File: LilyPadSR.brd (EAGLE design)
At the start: 100 x 50.9 mm, 40 parts, among them IC1 74HC595D, IC2 74HC595D

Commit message: alignment and routing
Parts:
- moved U$21 18.3 mm to (25.4, 76.8), turned to 270 degrees
- moved U$18 6.15 mm to (31.5, 75.9), turned to 253.7 degrees
- moved U$22 6.06 mm to (37.2, 73.4), turned to 237.4 degrees
- moved U$19 6.01 mm to (42.0, 69.3), turned to 221.1 degrees
- moved R13 2.75 mm to (32.8, 42.2)
- moved R16 2.54 mm to (39.6, 52.6)
- moved U$14 2.43 mm to (37.2, 35.8)
- moved U$15 2.37 mm to (42.0, 39.9)
- moved R15 2.34 mm to (38.6, 48.5)
- moved R14 2.17 mm to (36.3, 45.0)
- moved IC1 1.80 mm to (25.4, 59.7)
- moved IC2 1.80 mm to (25.4, 49.5)
- moved U$5 1.80 mm to (5.33, 64.0)
- moved U$16 1.80 mm to (45.5, 45.2)
- moved R12 1.63 mm to (29.2, 40.9)
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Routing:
- net VCC: track 0.00 -> 46.4 mm, vias 0 -> 4
- net GND: track 0.00 -> 44.9 mm
- net SRCLK: track 0.00 -> 23.0 mm
- net S_OUT: track 0.00 -> 19.2 mm
- net SER: track 0.00 -> 17.9 mm
- net RCLK: track 0.00 -> 17.7 mm
- net N$16: track 0.00 -> 15.1 mm, vias 0 -> 2
- net N$15: track 0.00 -> 14.4 mm
- net N$14: track 0.00 -> 13.7 mm
- net N$9: track 0.00 -> 13.4 mm
- net N$8: track 0.00 -> 12.9 mm
- net N$7: track 0.00 -> 12.4 mm
- net N$13: track 0.00 -> 11.7 mm
- net N$6: track 0.00 -> 10.7 mm
- net N$5: track 0.00 -> 10.4 mm
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
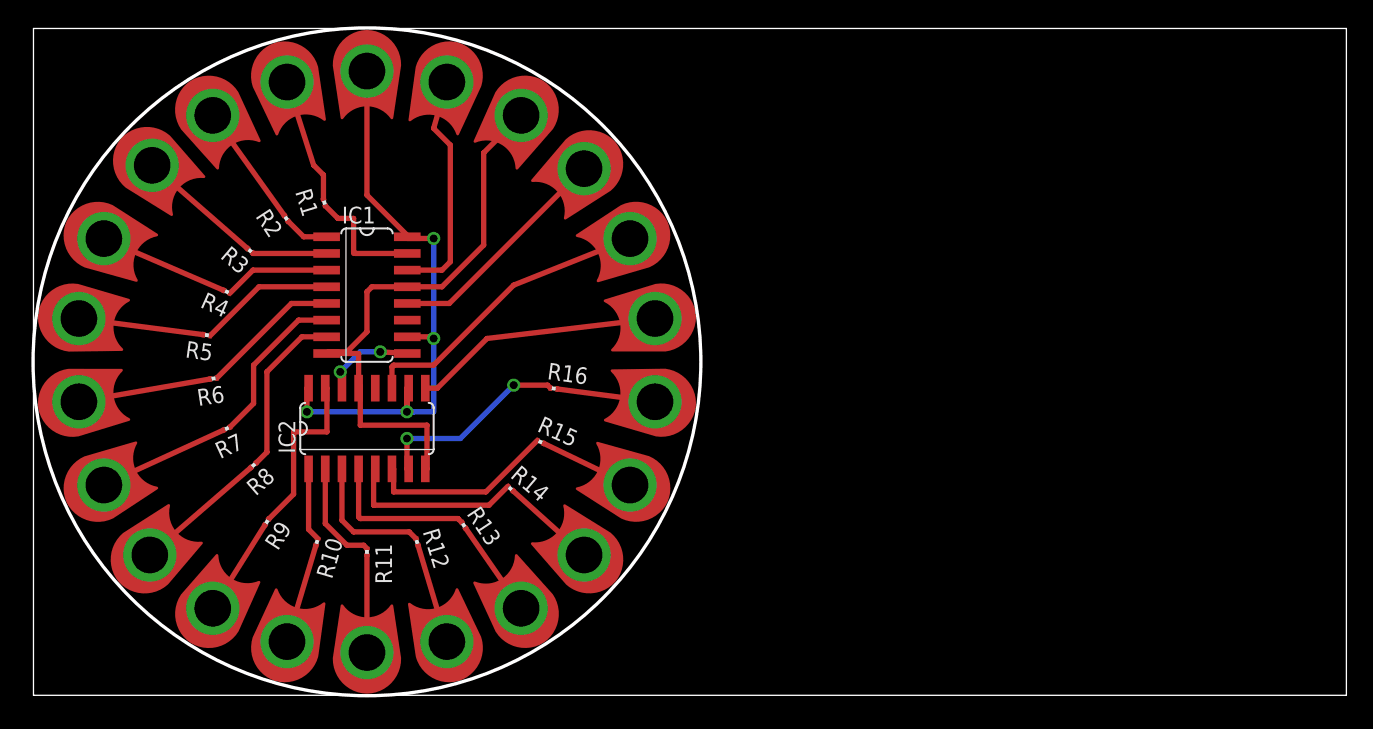
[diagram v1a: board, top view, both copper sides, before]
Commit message: removed right angles
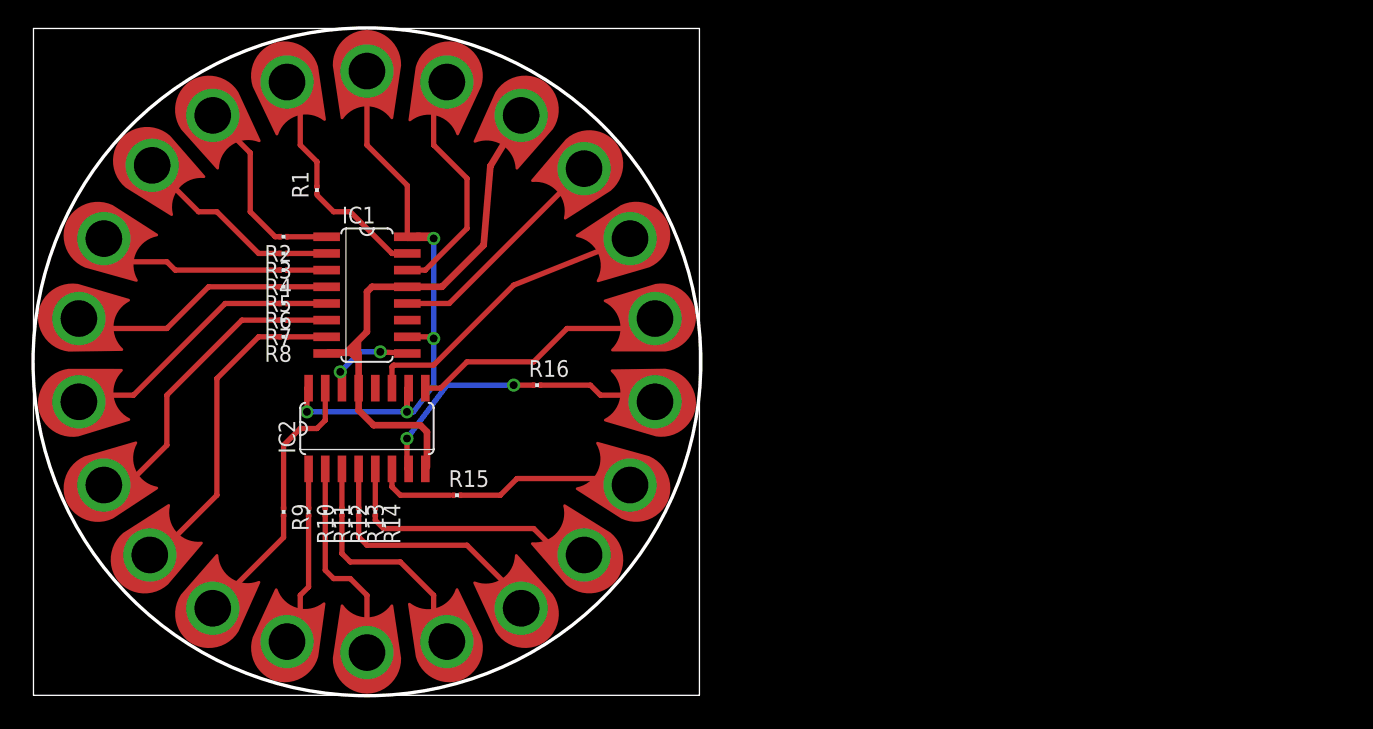
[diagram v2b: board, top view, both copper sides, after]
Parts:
- moved R14 10.4 mm to (26.0, 43.2), turned to 270 degrees
- moved R8 10.0 mm to (19.1, 56.5), turned to 180 degrees
- moved R7 9.32 mm to (19.1, 57.8), turned to 180 degrees
- moved R13 8.06 mm to (24.8, 43.2), turned to 270 degrees
- moved R6 7.82 mm to (19.1, 59.1), turned to 180 degrees
- moved R15 7.54 mm to (32.3, 44.5), turned to 0 degrees
- moved R5 6.91 mm to (19.1, 60.3), turned to 180 degrees
- moved R12 6.16 mm to (23.5, 43.2), turned to 270 degrees
- moved R4 4.62 mm to (19.1, 61.6), turned to 180 degrees
- moved R11 4.40 mm to (22.2, 43.2)
- moved R3 2.56 mm to (19.1, 62.9), turned to 180 degrees
- moved R10 2.37 mm to (21.0, 43.2), turned to 270 degrees
- moved R9 1.48 mm to (19.1, 43.2), turned to 270 degrees
- moved R2 1.41 mm to (19.1, 64.1), turned to 180 degrees
- moved R16 1.30 mm to (38.4, 52.8), turned to 0 degrees
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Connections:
- net N$18 renamed Q1
- net N$19 renamed Q2
- net N$20 renamed Q3
- net N$21 renamed Q4
- net N$22 renamed Q5
- net N$23 renamed Q6
- net N$24 renamed Q7
- net N$25 renamed Q8
- net N$26 renamed Q9
- net N$27 renamed Q10
- net N$28 renamed Q11
- net N$29 renamed Q12
- net N$30 renamed Q13
- net N$31 renamed Q14
- net N$32 renamed Q15
- net N$33 renamed Q16
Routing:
- net Q8: track 10.2 -> 22.0 mm
- net Q7: track 10.1 -> 20.9 mm
- net N$14: track 13.7 -> 3.02 mm
- net Q14: track 7.30 -> 17.4 mm
- net N$8: track 12.9 -> 3.02 mm
- net N$7: track 12.4 -> 3.02 mm
- net Q13: track 7.44 -> 16.7 mm
- net N$13: track 11.7 -> 3.03 mm
- net N$15: track 14.4 -> 6.08 mm
- net Q6: track 10.2 -> 18.4 mm
- net N$6: track 10.7 -> 3.02 mm
- net Q12: track 7.67 -> 15.2 mm
- net Q5: track 9.58 -> 17.0 mm
- net N$5: track 10.4 -> 3.02 mm
- net N$12: track 10.1 -> 3.02 mm
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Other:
- board size 100 x 50.9 mm -> 50.9 x 50.9 mm

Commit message: labelling
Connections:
- net VCC: no longer U$21.1
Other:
- board text added: "1"
- board text added: "10"
- board text added: "11"
- board text added: "12"
- board text added: "13"
- board text added: "14"
- board text added: "15"
- board text added: "16"
- board text added: "2"
- board text added: "3"
- board text added: "4"
- board text added: "5"
- board text added: "6"
- board text added: "7"
- board text added: "8"
- board text added: "9"
- board text added: "GND"
- board text added: "RCLK"
- board text added: "SER"
- board text added: "SOUT"
- board text added: "SRCLK"
- board text added: "Vin"
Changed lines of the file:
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@@
 <rectangle x1="24.384" y1="55.118" x2="24.765" y2="56.1594" layer="1"/>
 <rectangle x1="24.384" y1="55.118" x2="24.9682" y2="56.134" layer="1"/>
+<text x="20.32" y="70.612" size="1.27" layer="21">1</text>
+<text x="16.002" y="68.58" size="1.27" layer="21">2</text>
+<text x="12.446" y="65.532" size="1.27" layer="21">3</text>
+<text x="9.398" y="61.214" size="1.27" layer="21">4</text>
+<text x="7.874" y="56.388" size="1.27" layer="21">5</text>
+<text x="7.874" y="51.562" size="1.27" layer="21">6</text>
+<text x="9.398" y="46.482" size="1.27" layer="21">7</text>
+<text x="12.192" y="42.418" size="1.27" layer="21">8</text>
+<text x="12.192" y="42.418" size="1.27" layer="21">8</text>
+<text x="15.748" y="39.37" size="1.27" layer="21">9</text>
+<text x="19.558" y="37.338" size="1.27" layer="21">10</text>
+<text x="24.384" y="36.83" size="1.27" layer="21">11</text>
+<text x="28.956" y="37.338" size="1.27" layer="21">12</text>
+<text x="28.956" y="37.338" size="1.27" layer="21">12</text>
+<text x="33.274" y="39.37" size="1.27" layer="21">13</text>
+<text x="37.084" y="42.418" size="1.27" layer="21">14</text>
+<text x="39.624" y="46.482" size="1.27" layer="21">15</text>
+<text x="41.148" y="51.562" size="1.27" layer="21">16</text>
+<text x="24.13" y="71.12" size="1.27" layer="21">Vin</text>
+<text x="28.448" y="70.358" size="1.27" layer="21">SER</text>
+<text x="32.512" y="68.58" size="1.27" layer="21">GND</text>
+<text x="35.814" y="65.278" size="1.27" layer="21">RCLK</text>
+<text x="37.084" y="61.214" size="1.27" layer="21">SRCLK</text>
+<text x="39.37" y="56.388" size="1.27" layer="21">SOUT</text>
+<text x="23.622" y="63.754" size="0.762" layer="21">1</text>
+<text x="21.336" y="48.006" size="0.762" layer="21" rot="R90">1</text>
 </plain>
 <attributes>
@@
 <contactref element="IC2" pad="10"/>
 <contactref element="IC1" pad="10"/>
-<contactref element="U$21" pad="1"/>
 <wire x1="28.4734" y1="64.135" x2="28.4734" y2="64.008" width="0.4064" layer="1"/>
 <wire x1="28.4734" y1="64.008" x2="30.48" y2="64.008" width="0.4064" layer="1"/>
@@
 <via x="20.828" y="50.8" extent="1-16" drill="0.6" shape="square"/>
 <wire x1="20.828" y1="50.8" x2="28.448" y2="50.8" width="0.4064" layer="16"/>
-<wire x1="28.4734" y1="64.135" x2="28.4734" y2="68.0466" width="0.4064" layer="1"/>
-<wire x1="28.4734" y1="68.0466" x2="25.4" y2="71.12" width="0.4064" layer="1"/>
-<wire x1="25.4" y1="71.12" x2="25.4" y2="76.7542" width="0.4064" layer="1"/>
+<wire x1="28.4734" y1="64.135" x2="28.4734" y2="68.5546" width="0.4064" layer="1"/>
+<wire x1="25.4" y1="76.708" x2="25.4" y2="71.12" width="0" layer="19" extent="1-16"/>
 <wire x1="30.48" y1="64.262" x2="29.21" y2="64.262" width="0.4064" layer="1"/>
 <wire x1="30.48" y1="64.262" x2="30.48" y2="64.008" width="0.4064" layer="1"/>
+<wire x1="28.4734" y1="68.5546" x2="25.4" y2="71.628" width="0.4064" layer="1"/>
+<wire x1="25.4" y1="71.628" x2="25.4" y2="76.708" width="0.4064" layer="1"/>
 </signal>
 <signal name="N$2">

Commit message: design fixes and new job processed for batchpcb
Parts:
- moved U$16 0.11 mm to (45.5, 45.1)
- moved U$5 0.11 mm to (5.28, 64.1)
- moved U$10 0.08 mm to (13.6, 35.7)
- moved U$14 0.08 mm to (37.2, 35.7)
- moved U$20 0.08 mm to (45.5, 64.0)
- moved U$22 0.08 mm to (37.2, 73.5)
- moved U$3 0.08 mm to (13.6, 73.5)
- moved U$8 0.08 mm to (5.26, 45.2)
- moved U$9 0.08 mm to (8.76, 39.9)
- moved U$19 0.07 mm to (42.0, 69.4)
- moved U$12 0.05 mm to (25.4, 32.4)
- moved U$17 0.05 mm to (47.4, 51.6)
- moved U$21 0.05 mm to (25.4, 76.8)
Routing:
- net Q8: track 22.0 -> 22.8 mm
- net Q7: track 20.9 -> 21.4 mm

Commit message: minor fix
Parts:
- moved U$15 0.08 mm to (42.0, 39.9)
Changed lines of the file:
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@@
 <element name="U$13" library="LilyPad-Wearables" package="PETAL-LONG-1" value="SEWTAP1" x="31.496" y="33.2232" locked="yes" rot="R107"/>
 <element name="U$14" library="LilyPad-Wearables" package="PETAL-LONG-1" value="SEWTAP1" x="37.1602" y="35.7378" locked="yes" rot="R123.3"/>
-<element name="U$15" library="LilyPad-Wearables" package="PETAL-LONG-1" value="SEWTAP1" x="41.9608" y="39.878" locked="yes" rot="R139.6"/>
+<element name="U$15" library="LilyPad-Wearables" package="PETAL-LONG-1" value="SEWTAP1" x="42.037" y="39.878" locked="yes" rot="R139.6"/>
 <element name="U$16" library="LilyPad-Wearables" package="PETAL-LONG-1" value="SEWTAP1" x="45.5168" y="45.1104" locked="yes" rot="R155.9"/>
 <element name="U$17" library="LilyPad-Wearables" package="PETAL-LONG-1" value="SEWTAP1" x="47.4218" y="51.562" locked="yes" rot="R172.2"/>
@@
 <wire x1="38.1" y1="41.91" x2="39.37" y2="40.64" width="0.4064" layer="1"/>
 <wire x1="39.37" y1="40.64" x2="41.19539375" y2="40.64" width="0.4064" layer="1"/>
-<wire x1="41.19539375" y1="40.64" x2="41.937953125" y2="39.897440625" width="0.4064" layer="1"/>
+<wire x1="41.19539375" y1="40.64" x2="42.014153125" y2="39.897440625" width="0.4064" layer="1"/>
 </signal>
 <signal name="Q15">

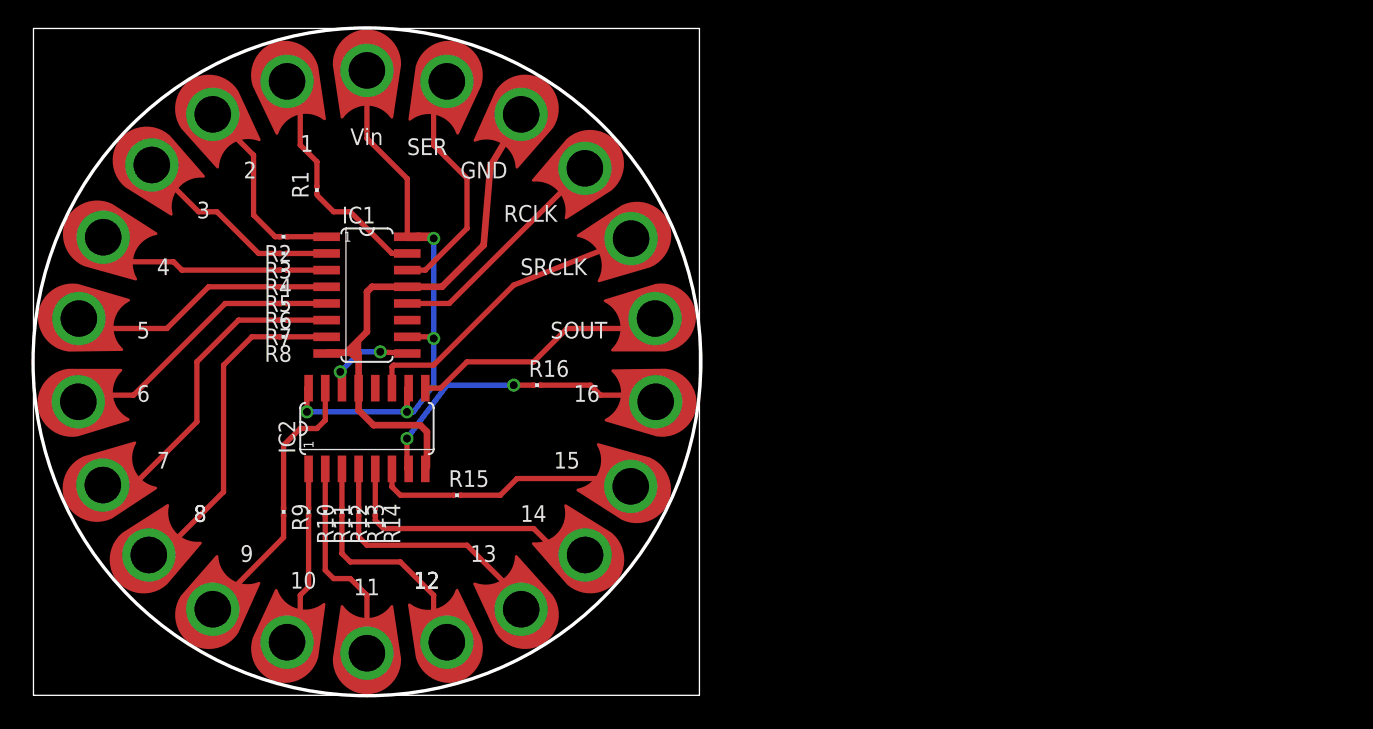
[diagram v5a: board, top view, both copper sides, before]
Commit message: switched 0201 resistors for 0805. removed gerber files, new ones to be generated
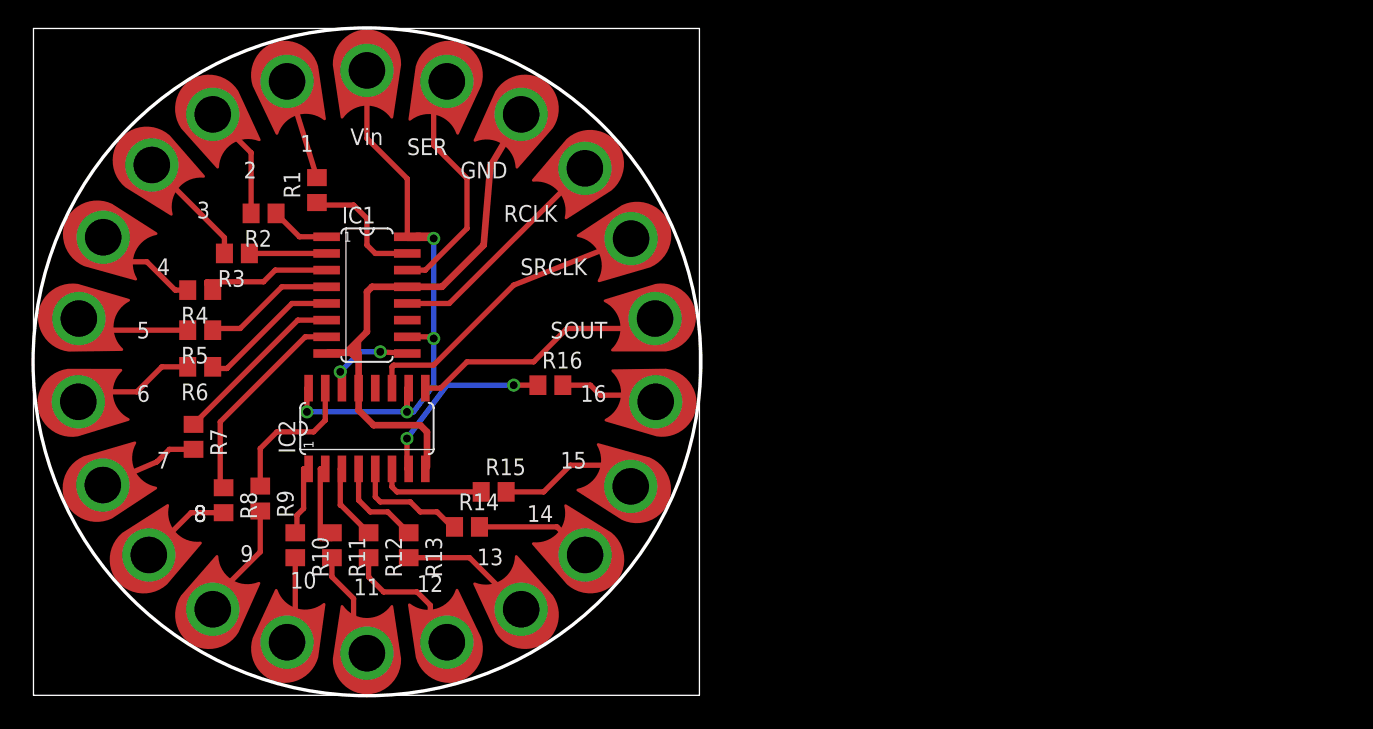
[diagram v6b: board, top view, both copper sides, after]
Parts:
- R1, R10, R11, R12, R13, R14, R15, R16, R2, R3, R4, R5, R6, R7, R8, R9: device rcl:R0201 -> rcl:R0805
- moved R8 13.3 mm to (14.5, 44.1), turned to 270 degrees
- moved R7 11.2 mm to (12.2, 48.9), turned to 270 degrees
- moved R6 7.98 mm to (12.7, 54.2)
- moved R5 7.16 mm to (12.7, 57.0)
- moved R14 7.08 mm to (33.0, 42.0), turned to 0 degrees
- moved R4 6.53 mm to (12.7, 60.1)
- moved R13 4.58 mm to (28.6, 40.6)
- moved R3 3.56 mm to (15.5, 62.9)
- moved R12 3.25 mm to (25.5, 40.6)
- moved R15 2.81 mm to (35.1, 44.7)
- moved R10 2.74 mm to (19.9, 40.6)
- moved R11 2.59 mm to (22.7, 40.6)
- moved R2 2.34 mm to (17.5, 65.9)
- moved R9 2.05 mm to (17.3, 44.2)
- moved R16 1.02 mm to (39.4, 52.8)
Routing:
- net Q8: track 22.8 -> 7.03 mm
- net Q7: track 21.4 -> 7.67 mm
- net N$8: track 3.02 -> 15.9 mm
- net N$7: track 3.02 -> 13.4 mm
- net Q6: track 18.5 -> 9.44 mm
- net Q14: track 17.4 -> 8.93 mm
- net Q5: track 17.0 -> 8.66 mm
- net N$6: track 3.02 -> 10.8 mm
- net N$4: track 3.02 -> 10.3 mm
- net N$5: track 3.02 -> 10.0 mm
- net Q13: track 16.7 -> 10.2 mm
- net Q4: track 14.5 -> 8.11 mm
- net N$14: track 3.02 -> 9.36 mm
- net Q12: track 15.2 -> 10.4 mm
- net N$13: track 3.03 -> 7.23 mm
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
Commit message: new design outputted and gerber generated
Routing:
- net N$11: track 7.02 -> 5.08 mm
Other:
- board size 50.9 x 50.9 mm -> 50.8 x 50.8 mm
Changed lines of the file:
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@@
 <wire x1="50.724" y1="80" x2="0" y2="80" width="0" layer="20"/>
 <wire x1="0" y1="80" x2="0" y2="29.21" width="0" layer="20"/>
-<circle x="25.4" y="54.61" radius="25.431728125" width="0.254" layer="20"/>
+<circle x="25.4" y="54.61" radius="25.4" width="0.254" layer="20"/>
 <rectangle x1="24.13" y1="55.372" x2="24.892" y2="55.88" layer="1"/>
 <rectangle x1="24.384" y1="55.118" x2="24.765" y2="56.1594" layer="1"/>
@@
 <contactref element="IC2" pad="1"/>
 <contactref element="R10" pad="1"/>
-<wire x1="20.955" y1="46.4566" x2="20.574" y2="46.4566" width="0.4064" layer="1"/>
-<wire x1="20.574" y1="46.4566" x2="20.574" y2="43.434" width="0.4064" layer="1"/>
-<wire x1="20.574" y1="43.434" x2="20.066" y2="42.926" width="0.4064" layer="1"/>
-<wire x1="20.066" y1="42.926" x2="20.066" y2="41.7169875" width="0.4064" layer="1"/>
+<wire x1="20.955" y1="46.4566" x2="20.955" y2="44.577" width="0.4064" layer="1"/>
+<wire x1="20.955" y1="44.577" x2="20.066" y2="43.688" width="0.4064" layer="1"/>
+<wire x1="20.066" y1="43.688" x2="20.066" y2="41.7169875" width="0.4064" layer="1"/>
 <wire x1="20.066" y1="41.7169875" x2="19.9390125" y2="41.59" width="0.4064" layer="1"/>
 </signal>
@@
 <contactref element="IC2" pad="2"/>
 <contactref element="R11" pad="1"/>
-<wire x1="22.225" y1="46.4566" x2="21.844" y2="46.4566" width="0.4064" layer="1"/>
-<wire x1="21.844" y1="46.4566" x2="21.844" y2="41.148" width="0.4064" layer="1"/>
-<wire x1="21.844" y1="41.148" x2="22.7312375" y2="41.148" width="0.4064" layer="1"/>
-<wire x1="22.7312375" y1="41.148" x2="22.7312375" y2="41.59" width="0.4064" layer="1"/>
+<wire x1="22.225" y1="46.4566" x2="22.225" y2="43.561" width="0.4064" layer="1"/>
+<wire x1="22.225" y1="43.561" x2="22.606" y2="43.18" width="0.4064" layer="1"/>
+<wire x1="22.606" y1="43.18" x2="22.606" y2="41.7152375" width="0.4064" layer="1"/>
+<wire x1="22.606" y1="41.7152375" x2="22.7312375" y2="41.59" width="0.4064" layer="1"/>
 </signal>
 <signal name="N$12">
 <contactref element="IC2" pad="3"/>
 <contactref element="R12" pad="1"/>
-<wire x1="23.495" y1="46.4566" x2="23.368" y2="46.4566" width="0.4064" layer="1"/>
-<wire x1="23.368" y1="46.4566" x2="23.368" y2="43.688" width="0.4064" layer="1"/>
-<wire x1="23.368" y1="43.688" x2="23.42830625" y2="43.688" width="0.4064" layer="1"/>
-<wire x1="23.42830625" y1="43.688" x2="25.52630625" y2="41.59" width="0.4064" layer="1"/>
+<wire x1="23.495" y1="46.4566" x2="23.495" y2="43.62130625" width="0.4064" layer="1"/>
+<wire x1="23.495" y1="43.62130625" x2="25.52630625" y2="41.59" width="0.4064" layer="1"/>
 </signal>
 <signal name="N$13">
